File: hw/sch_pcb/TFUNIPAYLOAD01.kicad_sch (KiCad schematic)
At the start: 78 parts, among them J1 SM06B-GHS-TB, J2 SM08B-GHS-TB, J3 HEADER_2x03, J4 SM04B-GHS-TB, J5 HEADER_2x15, J6 SM07B-GHS-TB, M1 HOLE, M2 HOLE, M3 HOLE, M4 HOLE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

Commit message: Routed PCB.
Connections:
- net PC5_D1 renamed LED1
- net PC6_D2 renamed LED2
- net PC7_D3 renamed LED3
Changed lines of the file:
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@@
 		)
 	)
-	(label "PC6_D2"
+	(label "LED2"
 		(at 233.68 125.73 0)
 		(effects
@@
 		)
 	)
-	(label "PC7_D3"
+	(label "LED3"
 		(at 308.61 97.79 0)
 		(effects
@@
 		)
 	)
-	(label "PC7_D3"
+	(label "LED3"
 		(at 233.68 128.27 0)
 		(effects
@@
 		)
 	)
-	(label "PC5_D1"
+	(label "LED1"
 		(at 358.14 92.71 0)
 		(effects
@@
 		)
 	)
-	(label "PC5_D1"
+	(label "LED1"
 		(at 233.68 123.19 0)
 		(effects
@@
 		)
 	)
-	(label "PC6_D2"
+	(label "LED2"
 		(at 306.07 72.39 0)
 		(effects

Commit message: Improve layout.
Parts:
- added G1: LOGO, TF_LOGA:TF, symbol TF_LOGO:LOGO
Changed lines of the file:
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@@
+	)
+	(symbol
+		(lib_id "TF_LOGO:LOGO")
+		(at 57.15 237.49 0)
+		(unit 1)
+		(exclude_from_sim no)
+		(in_bom no)
+		(on_board yes)
+		(dnp no)
+		(fields_autoplaced yes)
+		(property "Reference" "G1"
+			(at 72.39 237.4899 0)
+			(effects
+				(font
+					(size 1.27 1.27)
+				)
+				(justify left)
+			)
+		)
+		(property "Value" "LOGO"
+			(at 57.15 243.9576 0)
+			(effects
+				(font
+					(size 1.27 1.27)
+				)
+				(hide yes)
+			)
+		)
+		(property "Footprint" "TF_LOGA:TF"
+			(at 57.15 237.49 0)
+			(effects
+				(font
+					(size 1.27 1.27)
+				)
+				(hide yes)
+			)
+		)
+		(property "Datasheet" ""
+			(at 57.15 237.49 0)
+			(effects
+				(font
+					(size 1.27 1.27)
+				)
+				(hide yes)
+			)
+		)
+		(property "Description" ""
+			(at 57.15 237.49 0)
+			(effects
+				(font
+					(size 1.27 1.27)
+				)
+				(hide yes)
+			)
+		)
+		(property "UST_ID" ""
+			(at 57.15 237.49 0)
+			(effects
+				(font
+					(size 1.27 1.27)
+				)
+				(hide yes)
+			)
+		)
+		(instances
+			(project ""
+				(path "/0a87ced0-2af2-43c5-a56c-218f7013d76f"
+					(reference "G1")
+					(unit 1)
+				)
+			)
+		)
 	)
 	(symbol

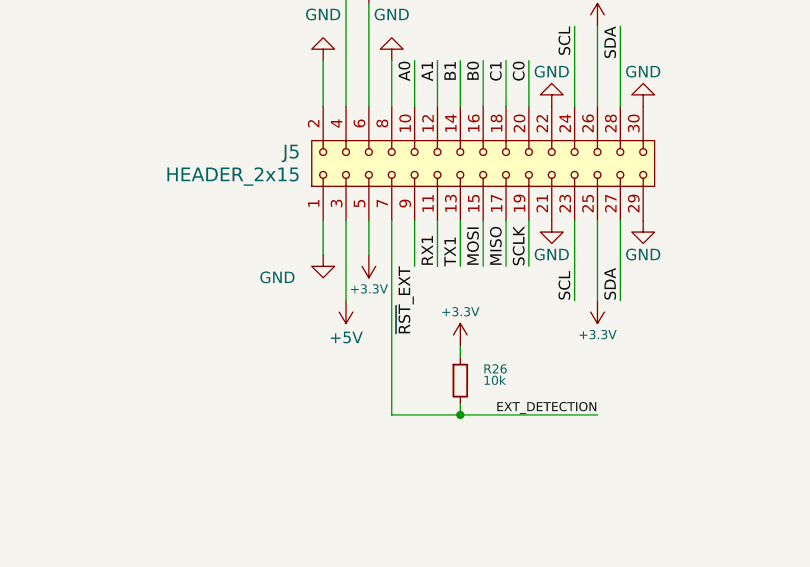
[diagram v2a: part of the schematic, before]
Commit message: Improve connector description.
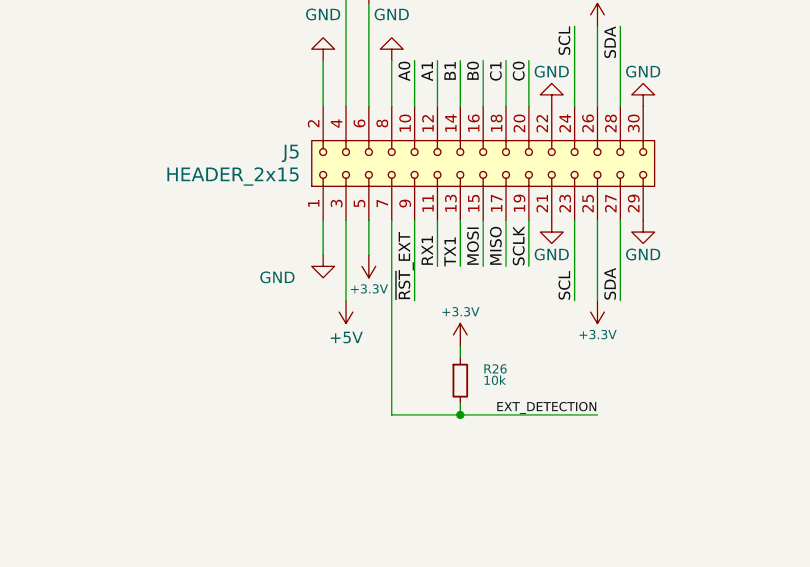
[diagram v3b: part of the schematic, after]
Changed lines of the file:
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@@
 	(wire
 		(pts
-			(xy 340.36 205.74) (xy 340.36 200.66)
+			(xy 340.36 209.55) (xy 340.36 200.66)
 		)
 		(stroke
@@
 	)
 	(label "~{RST}_EXT"
-		(at 340.36 205.74 270)
-		(effects
-			(font
-				(size 1.27 1.27)
-			)
-			(justify right bottom)
-		)
-	)
+		(at 340.36 209.55 90)
+		(effects
+			(font
+				(size 1.27 1.27)
+			)
+			(justify left bottom)
+		)
+	)

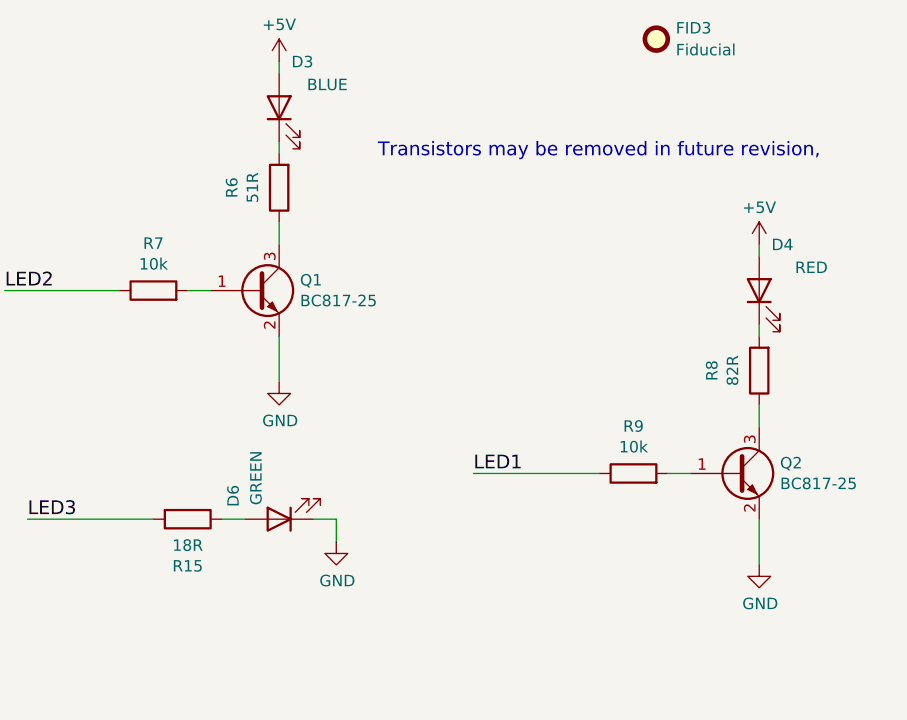
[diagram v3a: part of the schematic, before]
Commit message: Fix LED resistors values.
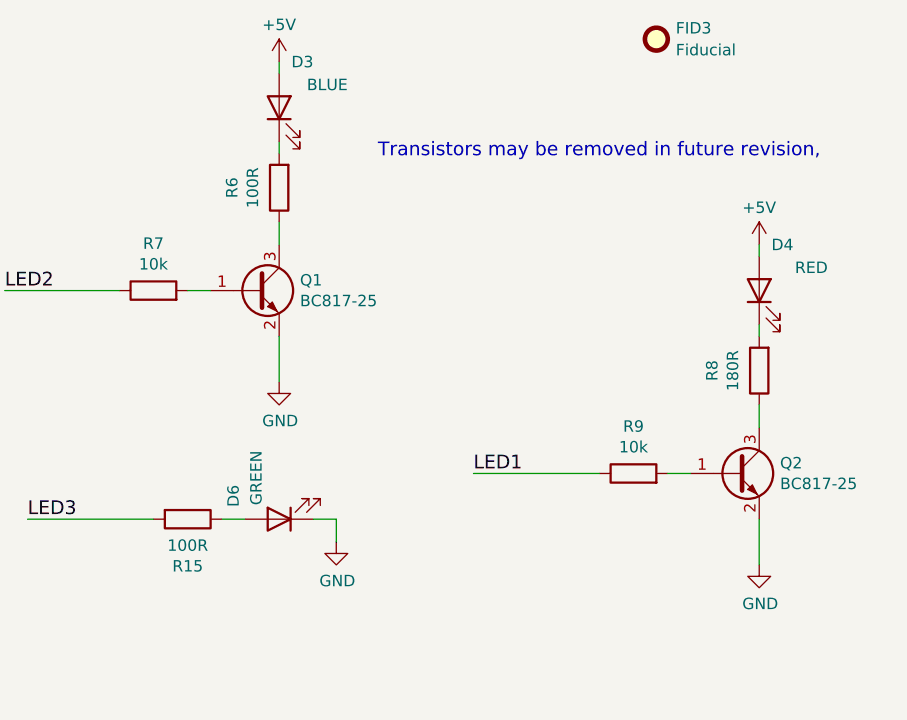
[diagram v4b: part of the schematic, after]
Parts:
- R15: value 18R -> 100R; UST_ID 5c70984512875079b91f896e -> 5c70984512875079b91f8956
- R6: value 51R -> 100R; UST_ID 5c70984512875079b91f8953 -> 5c70984512875079b91f8956
- R8: value 82R -> 180R; UST_ID 5c70984512875079b91f8976 -> 5c70984512875079b91f897c
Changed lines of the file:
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@@
 			)
 		)
-		(property "Datasheet" "~"
+		(property "Datasheet" "https://v4.cecdn.yun300.cn/100001_2003185297/17%20FYLS-1206XXXC-D.pdf"
 			(at 336.55 52.07 0)
 			(effects
@@
 			)
 		)
-		(property "Value" "18R"
+		(property "Value" "100R"
 			(at 326.39 100.717 90)
 			(effects
@@
 			)
 		)
-		(property "UST_ID" "5c70984512875079b91f896e"
+		(property "UST_ID" "5c70984512875079b91f8956"
 			(at 326.39 97.79 0)
 			(effects
@@
 			)
 		)
-		(property "Value" "51R"
+		(property "Value" "100R"
 			(at 333.623 60.96 90)
 			(effects
@@
 			)
 		)
-		(property "UST_ID" "5c70984512875079b91f8953"
+		(property "UST_ID" "5c70984512875079b91f8956"
 			(at 336.55 60.96 0)
 			(effects
@@
 			)
 		)
-		(property "Value" "82R"
+		(property "Value" "180R"
 			(at 386.963 81.28 90)
 			(effects
@@
 			)
 		)
-		(property "UST_ID" "5c70984512875079b91f8976"
+		(property "UST_ID" "5c70984512875079b91f897c"
 			(at 389.89 81.28 0)
 			(effects
